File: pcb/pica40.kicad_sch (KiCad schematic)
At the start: 63 parts, among them SW1 SW_PUSH, SW10 SW_PUSH, SW11 SW_PUSH, SW12 SW_PUSH, SW13 SW_PUSH, SW14 SW_PUSH, SW15 SW_PUSH, SW16 SW_PUSH, SW17 SW_PUSH, SW18 SW_PUSH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

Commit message: fixes
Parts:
- D1, D10, D11, D12, D13, D14, D15, D16, D17, D18, D19, D2, D20, D3, D4, D5, D6, D7, D8, D9: footprint pica:D_SOD123 -> pica:D3_SMD
- LED1: footprint keebio:SK6812-MINI-E -> pica:SK6812-MINI-E
- RE1: footprint keebio:RotaryEncoder_EC11-no-legs -> pica:RotaryEncoder_EC11-no-legs
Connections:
- net GND: now also LED1.3 (VSS); no longer LED1.1 (VDD)
- net VCC: now also LED1.1 (VDD); no longer LED1.3 (VSS)
- no-connect marks 6 -> 7

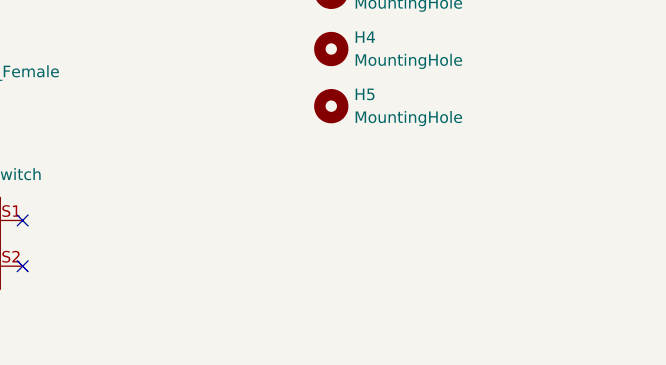
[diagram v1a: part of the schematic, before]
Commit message: add breakaway plate, replace battery connector
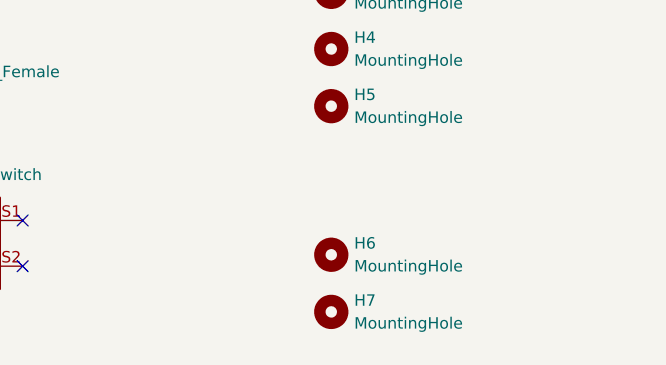
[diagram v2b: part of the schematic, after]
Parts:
- added H6, H7: MountingHole, kbd:M2_Hole_TH, symbol Mechanical:MountingHole
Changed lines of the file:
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@@
     (pin "2")
+  )
+  (symbol (lib_id "Mechanical:MountingHole") (at 237.49 158.75 0) (unit 1)
+    (in_bom yes) (on_board yes) (fields_autoplaced)
+    (property "Reference" "H7" (id 0) (at 240.03 157.4799 0)
+      (effects (font (size 1.27 1.27)) (justify left))
+    )
+    (property "Value" "MountingHole" (id 1) (at 240.03 160.0199 0)
+      (effects (font (size 1.27 1.27)) (justify left))
+    )
+    (property "Footprint" "kbd:M2_Hole_TH" (id 2) (at 237.49 158.75 0)
+      (effects (font (size 1.27 1.27)) hide)
+    )
+    (property "Datasheet" "~" (id 3) (at 237.49 158.75 0)
+      (effects (font (size 1.27 1.27)) hide)
+    )
   )
   (symbol (lib_id "kbd:OLED") (at 248.92 40.64 0) (unit 1)
@@
     (pin "2")
   )
+  (symbol (lib_id "Mechanical:MountingHole") (at 237.49 152.4 0) (unit 1)
+    (in_bom yes) (on_board yes) (fields_autoplaced)
+    (property "Reference" "H6" (id 0) (at 240.03 151.1299 0)
+      (effects (font (size 1.27 1.27)) (justify left))
+    )
+    (property "Value" "MountingHole" (id 1) (at 240.03 153.6699 0)
+      (effects (font (size 1.27 1.27)) (justify left))
+    )
+    (property "Footprint" "kbd:M2_Hole_TH" (id 2) (at 237.49 152.4 0)
+      (effects (font (size 1.27 1.27)) hide)
+    )
+    (property "Datasheet" "~" (id 3) (at 237.49 152.4 0)
+      (effects (font (size 1.27 1.27)) hide)
+    )
+  )
   (symbol (lib_id "kbd:YS-SK6812MINI-E") (at 250.19 88.9 0) (unit 1)
     (in_bom yes) (on_board yes)
@@
       (reference "H5") (unit 1) (value "MountingHole") (footprint "kbd:M2_HOLE_v2")
     )
+    (path "/f52c0b43-7ef2-43de-9e7f-2633ce8cd351"
+      (reference "H6") (unit 1) (value "MountingHole") (footprint "kbd:M2_Hole_TH")
+    )
+    (path "/dc3229c7-5794-49f0-b14b-ffc46123b28f"
+      (reference "H7") (unit 1) (value "MountingHole") (footprint "kbd:M2_Hole_TH")
+    )
     (path "/a9c8cfb2-a37f-4ce1-a05d-b4bc62a7b38f"

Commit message: update and reroute
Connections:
- net col1: now also U1.12 (9/B5); no longer U1.20 (F4/A3)
- net col2: now also U1.11 (8/B4); no longer U1.19 (F5/A2)
- net col3: now also U1.10 (7/E6); no longer U1.18 (F6/A1)
- net col4: now also U1.9 (6/D7); no longer U1.17 (F7/A0)
- net row4: now also U1.17 (F7/A0); no longer U1.12 (9/B5)
- net row5: now also U1.18 (F6/A1); no longer U1.11 (8/B4)
- net row6: now also U1.19 (F5/A2); no longer U1.10 (7/E6)
- net row7: now also U1.20 (F4/A3); no longer U1.9 (6/D7)
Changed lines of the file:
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@@
     )
   )
-  (global_label "col1" (shape input) (at 69.85 45.72 0) (fields_autoplaced)
-    (effects (font (size 1.27 1.27)) (justify left))
-    (property "Intersheet References" "${INTERSHEET_REFS}" (id 0) (at 76.3755 45.7994 0)
-      (effects (font (size 1.27 1.27)) (justify left) hide)
+  (global_label "col1" (shape input) (at 34.29 63.5 180) (fields_autoplaced)
+    (effects (font (size 1.27 1.27)) (justify right))
+    (property "Intersheet References" "${INTERSHEET_REFS}" (id 0) (at 27.7645 63.4206 0)
+      (effects (font (size 1.27 1.27)) (justify right) hide)
     )
   )
@@
     )
   )
-  (global_label "col4" (shape input) (at 69.85 53.34 0) (fields_autoplaced)
-    (effects (font (size 1.27 1.27)) (justify left))
-    (property "Intersheet References" "${INTERSHEET_REFS}" (id 0) (at 76.3755 53.4194 0)
-      (effects (font (size 1.27 1.27)) (justify left) hide)
-    )
-  )
-  (global_label "row5" (shape input) (at 34.29 60.96 180) (fields_autoplaced)
-    (effects (font (size 1.27 1.27)) (justify right))
-    (property "Intersheet References" "${INTERSHEET_REFS}" (id 0) (at 27.4017 61.0394 0)
-      (effects (font (size 1.27 1.27)) (justify right) hide)
+  (global_label "col4" (shape input) (at 34.29 55.88 180) (fields_autoplaced)
+    (effects (font (size 1.27 1.27)) (justify right))
+    (property "Intersheet References" "${INTERSHEET_REFS}" (id 0) (at 27.7645 55.8006 0)
+      (effects (font (size 1.27 1.27)) (justify right) hide)
+    )
+  )
+  (global_label "row5" (shape input) (at 69.85 50.8 0) (fields_autoplaced)
+    (effects (font (size 1.27 1.27)) (justify left))
+    (property "Intersheet References" "${INTERSHEET_REFS}" (id 0) (at 76.7383 50.7206 0)
+      (effects (font (size 1.27 1.27)) (justify left) hide)
     )
   )
@@
     )
   )
-  (global_label "col2" (shape input) (at 69.85 48.26 0) (fields_autoplaced)
-    (effects (font (size 1.27 1.27)) (justify left))
-    (property "Intersheet References" "${INTERSHEET_REFS}" (id 0) (at 76.3755 48.3394 0)
-      (effects (font (size 1.27 1.27)) (justify left) hide)
+  (global_label "col2" (shape input) (at 34.29 60.96 180) (fields_autoplaced)
+    (effects (font (size 1.27 1.27)) (justify right))
+    (property "Intersheet References" "${INTERSHEET_REFS}" (id 0) (at 27.7645 60.8806 0)
+      (effects (font (size 1.27 1.27)) (justify right) hide)
     )
   )
@@
     )
   )
-  (global_label "row6" (shape input) (at 34.29 58.42 180) (fields_autoplaced)
-    (effects (font (size 1.27 1.27)) (justify right))
-    (property "Intersheet References" "${INTERSHEET_REFS}" (id 0) (at 27.4017 58.4994 0)
-      (effects (font (size 1.27 1.27)) (justify right) hide)
+  (global_label "row6" (shape input) (at 69.85 48.26 0) (fields_autoplaced)
+    (effects (font (size 1.27 1.27)) (justify left))
+    (property "Intersheet References" "${INTERSHEET_REFS}" (id 0) (at 76.7383 48.1806 0)
+      (effects (font (size 1.27 1.27)) (justify left) hide)
     )
   )
@@
     )
   )
-  (global_label "col3" (shape input) (at 69.85 50.8 0) (fields_autoplaced)
-    (effects (font (size 1.27 1.27)) (justify left))
-    (property "Intersheet References" "${INTERSHEET_REFS}" (id 0) (at 76.3755 50.8794 0)
-      (effects (font (size 1.27 1.27)) (justify left) hide)
+  (global_label "col3" (shape input) (at 34.29 58.42 180) (fields_autoplaced)
+    (effects (font (size 1.27 1.27)) (justify right))
+    (property "Intersheet References" "${INTERSHEET_REFS}" (id 0) (at 27.7645 58.3406 0)
+      (effects (font (size 1.27 1.27)) (justify right) hide)
     )
   )
@@
     )
   )
-  (global_label "row4" (shape input) (at 34.29 63.5 180) (fields_autoplaced)
-    (effects (font (size 1.27 1.27)) (justify right))
-    (property "Intersheet References" "${INTERSHEET_REFS}" (id 0) (at 27.4017 63.5794 0)
-      (effects (font (size 1.27 1.27)) (justify right) hide)
+  (global_label "row4" (shape input) (at 69.85 53.34 0) (fields_autoplaced)
+    (effects (font (size 1.27 1.27)) (justify left))
+    (property "Intersheet References" "${INTERSHEET_REFS}" (id 0) (at 76.7383 53.2606 0)
+      (effects (font (size 1.27 1.27)) (justify left) hide)
     )
   )
@@
     )
   )
-  (global_label "row7" (shape input) (at 34.29 55.88 180) (fields_autoplaced)
-    (effects (font (size 1.27 1.27)) (justify right))
-    (property "Intersheet References" "${INTERSHEET_REFS}" (id 0) (at 27.4017 55.9594 0)
-      (effects (font (size 1.27 1.27)) (justify right) hide)
-    )
-  )
+  (global_label "row7" (shape input) (at 69.85 45.72 0) (fields_autoplaced)
+    (effects (font (size 1.27 1.27)) (justify left))
+    (property "Intersheet References" "${INTERSHEET_REFS}" (id 0) (at 76.7383 45.6406 0)
+      (effects (font (size 1.27 1.27)) (justify left) hide)
+    )
+  )
